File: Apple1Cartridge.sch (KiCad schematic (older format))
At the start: 16 parts

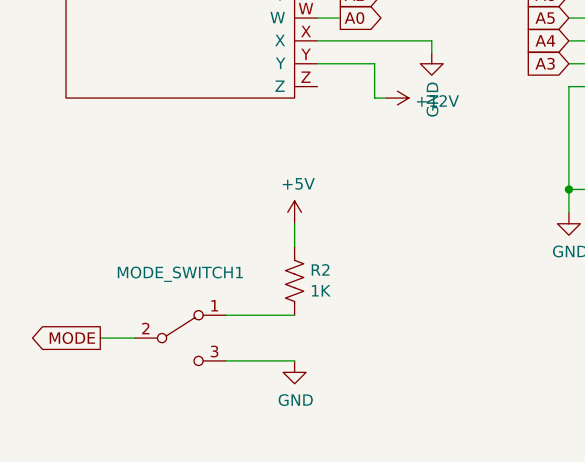
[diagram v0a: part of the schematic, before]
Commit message: Fixed element values on schematics
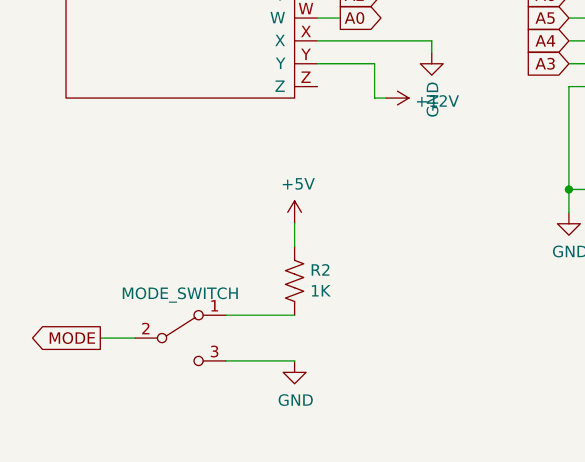
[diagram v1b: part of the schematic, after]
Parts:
- BANK1: footprint Package_DIP:DIP-14_W7.62mm_Socket_LongPads -> Package_DIP:DIP-14_W7.62mm_LongPads
- DECODER1: footprint Package_DIP:DIP-24_W7.62mm_Socket_LongPads -> Package_DIP:DIP-24_W7.62mm_LongPads
- MODE_SWITCH1: value SW_SPDT -> MODE_SWITCH
- RAM1, ROM1: footprint Package_DIP:DIP-28_W15.24mm_Socket_LongPads -> Package_DIP:DIP-28_W15.24mm_LongPads
- RAM2: footprint Package_DIP:DIP-28_W15.24mm_Socket -> Package_DIP:DIP-28_W15.24mm
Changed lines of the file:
@@
 F 0 "DECODER1" H 3950 5115 50  0000 C CNN
 F 1 "GAL22V10" H 3950 5024 50  0000 C CNN
-F 2 "Package_DIP:DIP-24_W7.62mm_Socket_LongPads" H 4350 4950 50  0001 L CNN
+F 2 "Package_DIP:DIP-24_W7.62mm_LongPads" H 4350 4950 50  0001 L CNN
 F 3 "" H 4350 4850 50  0001 L CNN
 F 4 "Lattice Semiconductor GAL22V10-15LP, SPLD GAL, GAL20V8B 8 Macro Cells, 8 I/O, 62.5MHz External 15ns EECMOS 24-Pin PDIP" H 4350 4750 50  0001 L CNN "Description"
@@
 F 0 "ROM1" H 4250 2665 50  0000 C CNN
 F 1 "28C256" H 4250 2574 50  0000 C CNN
-F 2 "Package_DIP:DIP-28_W15.24mm_Socket_LongPads" H 4650 2500 50  0001 L CNN
+F 2 "Package_DIP:DIP-28_W15.24mm_LongPads" H 4650 2500 50  0001 L CNN
 F 3 "http://www.atmel.com/images/doc0270.pdf" H 4650 2400 50  0001 L CNN
 	1    3700 2400
@@
 F 0 "RAM1" H 6350 2665 50  0000 C CNN
 F 1 "62256" H 6350 2574 50  0000 C CNN
-F 2 "Package_DIP:DIP-28_W15.24mm_Socket_LongPads" H 6750 2500 50  0001 L CNN
+F 2 "Package_DIP:DIP-28_W15.24mm_LongPads" H 6750 2500 50  0001 L CNN
 F 3 "http://www.atmel.com/images/doc0270.pdf" H 6750 2400 50  0001 L CNN
 	1    5800 2400
@@
 F 0 "BANK1" H 6400 6231 50  0000 C CNN
 F 1 "74LS74" H 6400 6140 50  0000 C CNN
-F 2 "Package_DIP:DIP-14_W7.62mm_Socket_LongPads" H 6400 5750 50  0001 C CNN
+F 2 "Package_DIP:DIP-14_W7.62mm_LongPads" H 6400 5750 50  0001 C CNN
 F 3 "74xx/74hc_hct74.pdf" H 6400 5750 50  0001 C CNN
 	1    6400 5750
@@
 F 0 "BANK1" H 7730 5696 50  0000 L CNN
 F 1 "74LS74" H 7730 5605 50  0000 L CNN
-F 2 "Package_DIP:DIP-14_W7.62mm_Socket_LongPads" H 7500 5650 50  0001 C CNN
+F 2 "Package_DIP:DIP-14_W7.62mm_LongPads" H 7500 5650 50  0001 C CNN
 F 3 "74xx/74hc_hct74.pdf" H 7500 5650 50  0001 C CNN
 	3    7500 5650
@@
 U 1 1 5F232F13
 P 1600 7050
-F 0 "MODE_SWITCH1" H 1600 7335 50  0000 C CNN
-F 1 "SW_SPDT" H 1600 7244 50  0001 C CNN
+F 0 "MODE_SWITCH1" H 1600 7335 50  0001 C CNN
+F 1 "MODE_SWITCH" H 1600 7244 50  0000 C CNN
 F 2 "Connector_PinHeader_2.54mm:PinHeader_1x03_P2.54mm_Vertical" H 1600 7050 50  0001 C CNN
 F 3 "~" H 1600 7050 50  0001 C CNN
@@
 F 0 "RAM2" H 9000 2665 50  0000 C CNN
 F 1 "62256" H 9000 2574 50  0000 C CNN
-F 2 "Package_DIP:DIP-28_W15.24mm_Socket" H 9400 2500 50  0001 L CNN
+F 2 "Package_DIP:DIP-28_W15.24mm" H 9400 2500 50  0001 L CNN
 F 3 "http://www.atmel.com/images/doc0270.pdf" H 9400 2400 50  0001 L CNN
 	1    8450 2400
